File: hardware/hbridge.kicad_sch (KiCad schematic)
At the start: 11 parts, among them U601 BTS7960B, U602 BTS7960B

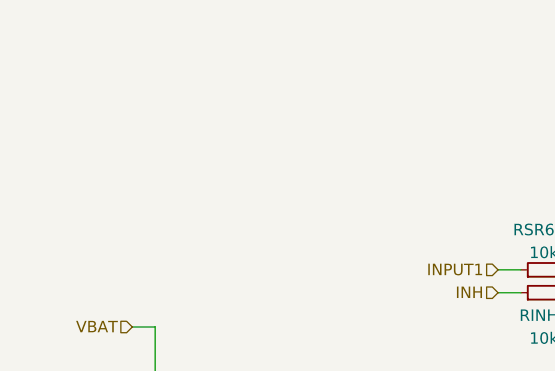
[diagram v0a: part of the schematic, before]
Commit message: Added analog stage for Vbat measurement, and it's simulation
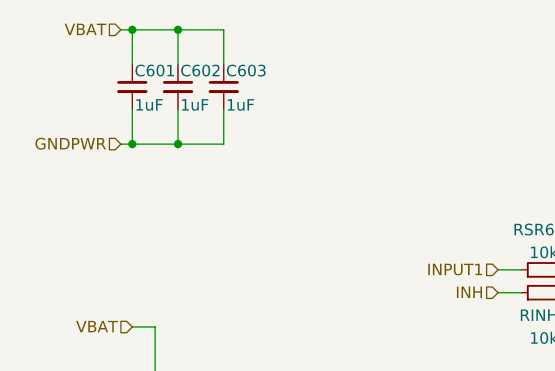
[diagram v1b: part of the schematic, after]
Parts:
- added C601, C602, C603: 1uF, Capacitor_SMD:C_1206_3216Metric_Pad1.33x1.80mm_HandSolder, symbol Device:C_Small
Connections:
- net GNDPWR: now also C601.2, C602.2, C603.2
- net VBAT: now also C601.1, C602.1, C603.1
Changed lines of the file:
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@@
 (kicad_sch (version 20211123) (generator eeschema)
   (paper "A4")
+  (junction (at 52.07 50.8) (diameter 0) (color 0 0 0 0)
+  )
+  (junction (at 57.15 38.1) (diameter 0) (color 0 0 0 0)
+  )
+  (junction (at 57.15 50.8) (diameter 0) (color 0 0 0 0)
+  )
   (junction (at 54.61 78.74) (diameter 0) (color 0 0 0 0)
   )
+  (junction (at 52.07 38.1) (diameter 0) (color 0 0 0 0)
+  )
   (junction (at 54.61 97.79) (diameter 0) (color 0 0 0 0)
   )
@@
     (stroke (width 0) (type default) (color 0 0 0 0))
   )
+  (wire (pts (xy 57.15 50.8) (xy 52.07 50.8))
+    (stroke (width 0) (type default) (color 0 0 0 0))
+  )
+  (wire (pts (xy 57.15 41.91) (xy 57.15 38.1))
+    (stroke (width 0) (type default) (color 0 0 0 0))
+  )
   (wire (pts (xy 54.61 71.12) (xy 52.07 71.12))
     (stroke (width 0) (type default) (color 0 0 0 0))
   )
+  (wire (pts (xy 62.23 38.1) (xy 62.23 41.91))
+    (stroke (width 0) (type default) (color 0 0 0 0))
+  )
   (wire (pts (xy 107.95 114.3) (xy 109.22 114.3))
     (stroke (width 0) (type default) (color 0 0 0 0))
@@
     (stroke (width 0) (type default) (color 0 0 0 0))
   )
+  (wire (pts (xy 52.07 46.99) (xy 52.07 50.8))
+    (stroke (width 0) (type default) (color 0 0 0 0))
+  )
   (wire (pts (xy 149.86 114.3) (xy 152.4 114.3))
     (stroke (width 0) (type default) (color 0 0 0 0))
@@
     (stroke (width 0) (type default) (color 0 0 0 0))
   )
+  (wire (pts (xy 50.8 38.1) (xy 52.07 38.1))
+    (stroke (width 0) (type default) (color 0 0 0 0))
+  )
+  (wire (pts (xy 57.15 38.1) (xy 62.23 38.1))
+    (stroke (width 0) (type default) (color 0 0 0 0))
+  )
   (wire (pts (xy 100.33 67.31) (xy 110.49 67.31))
     (stroke (width 0) (type default) (color 0 0 0 0))
@@
     (stroke (width 0) (type default) (color 0 0 0 0))
   )
+  (wire (pts (xy 62.23 46.99) (xy 62.23 50.8))
+    (stroke (width 0) (type default) (color 0 0 0 0))
+  )
   (wire (pts (xy 107.95 69.85) (xy 110.49 69.85))
     (stroke (width 0) (type default) (color 0 0 0 0))
@@
     (stroke (width 0) (type default) (color 0 0 0 0))
   )
+  (wire (pts (xy 57.15 46.99) (xy 57.15 50.8))
+    (stroke (width 0) (type default) (color 0 0 0 0))
+  )
   (wire (pts (xy 92.71 111.76) (xy 95.25 111.76))
     (stroke (width 0) (type default) (color 0 0 0 0))
@@
     (stroke (width 0) (type default) (color 0 0 0 0))
   )
+  (wire (pts (xy 52.07 41.91) (xy 52.07 38.1))
+    (stroke (width 0) (type default) (color 0 0 0 0))
+  )
   (wire (pts (xy 153.67 76.2) (xy 153.67 78.74))
     (stroke (width 0) (type default) (color 0 0 0 0))
@@
     (stroke (width 0) (type default) (color 0 0 0 0))
   )
+  (wire (pts (xy 52.07 38.1) (xy 57.15 38.1))
+    (stroke (width 0) (type default) (color 0 0 0 0))
+  )
   (wire (pts (xy 48.26 85.09) (xy 48.26 78.74))
     (stroke (width 0) (type default) (color 0 0 0 0))
@@
     (stroke (width 0) (type default) (color 0 0 0 0))
   )
+  (wire (pts (xy 62.23 50.8) (xy 57.15 50.8))
+    (stroke (width 0) (type default) (color 0 0 0 0))
+  )
   (wire (pts (xy 185.42 77.47) (xy 185.42 81.28))
+    (stroke (width 0) (type default) (color 0 0 0 0))
+  )
+  (wire (pts (xy 52.07 50.8) (xy 50.8 50.8))
     (stroke (width 0) (type default) (color 0 0 0 0))
   )
@@
     (effects (font (size 1.27 1.27)) (justify right))
   )
+  (hierarchical_label "VBAT" (shape input) (at 50.8 38.1 180)
+    (effects (font (size 1.27 1.27)) (justify right))
+  )
   (hierarchical_label "VBAT" (shape input) (at 52.07 71.12 180)
     (effects (font (size 1.27 1.27)) (justify right))
   )
+  (hierarchical_label "GNDPWR" (shape input) (at 50.8 50.8 180)
+    (effects (font (size 1.27 1.27)) (justify right))
+  )
   (hierarchical_label "IS" (shape input) (at 185.42 77.47 180)
     (effects (font (size 1.27 1.27)) (justify right))
@@
   (hierarchical_label "OUT2" (shape input) (at 107.95 93.98 180)
     (effects (font (size 1.27 1.27)) (justify right))
+  )
+  (symbol (lib_id "Device:C_Small") (at 57.15 44.45 0) (unit 1)
+    (in_bom yes) (on_board yes)
+    (property "Reference" "C602" (id 0) (at 57.404 42.672 0)
+      (effects (font (size 1.27 1.27)) (justify left))
+    )
+    (property "Value" "1uF" (id 1) (at 57.404 46.482 0)
+      (effects (font (size 1.27 1.27)) (justify left))
+    )
+    (property "Footprint" "Capacitor_SMD:C_1206_3216Metric_Pad1.33x1.80mm_HandSolder" (id 2) (at 57.15 44.45 0)
+      (effects (font (size 1.27 1.27)) hide)
+    )
+    (property "Datasheet" "" (id 3) (at 57.15 44.45 0)
+      (effects (font (size 1.27 1.27)) hide)
+    )
+    (pin "1")
+    (pin "2")
   )
   (symbol (lib_id "power:GND") (at 185.42 88.9 0) (unit 1)
@@
     (pin "2")
   )
+  (symbol (lib_id "Device:C_Small") (at 52.07 44.45 0) (unit 1)
+    (in_bom yes) (on_board yes)
+    (property "Reference" "C601" (id 0) (at 52.324 42.672 0)
+      (effects (font (size 1.27 1.27)) (justify left))
+    )
+    (property "Value" "1uF" (id 1) (at 52.324 46.482 0)
+      (effects (font (size 1.27 1.27)) (justify left))
+    )
+    (property "Footprint" "Capacitor_SMD:C_1206_3216Metric_Pad1.33x1.80mm_HandSolder" (id 2) (at 52.07 44.45 0)
+      (effects (font (size 1.27 1.27)) hide)
+    )
+    (property "Datasheet" "" (id 3) (at 52.07 44.45 0)
+      (effects (font (size 1.27 1.27)) hide)
+    )
+    (pin "1")
+    (pin "2")
+  )
   (symbol (lib_id "Device:R_Small") (at 97.79 64.77 90) (unit 1)
     (in_bom yes) (on_board yes) (fields_autoplaced)
@@
       (effects (font (size 1.27 1.27)) hide)
     )
+    (pin "1")
+    (pin "2")
+  )
+  (symbol (lib_id "Device:C_Small") (at 62.23 44.45 0) (unit 1)
+    (in_bom yes) (on_board yes)
+    (property "Reference" "C603" (id 0) (at 62.484 42.672 0)
+      (effects (font (size 1.27 1.27)) (justify left))
+    )
+    (property "Value" "1uF" (id 1) (at 62.484 46.482 0)
+      (effects (font (size 1.27 1.27)) (justify left))
+    )
+    (property "Footprint" "Capacitor_SMD:C_1206_3216Metric_Pad1.33x1.80mm_HandSolder" (id 2) (at 62.23 44.45 0)
+      (effects (font (size 1.27 1.27)) hide)
+    )
+    (property "Datasheet" "" (id 3) (at 62.23 44.45 0)
+      (effects (font (size 1.27 1.27)) hide)
+    )

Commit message: hardware: K78L15 to supply INA826 and other changes
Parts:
- added C604: (no value), symbol Device:C_Polarized_Small
- added C605, C606: C_Polarized_Small, Capacitor_SMD:CP_Elec_8x10, symbol Device:C_Polarized_Small
- added RIS601: (no value), symbol Device:R_Small
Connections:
- net GND: now also RIS601.2
- net GNDPWR: now also C604.2, C605.2, C606.2
- net VBAT: now also C604.1, C605.1, C606.1
- net IS renamed IS1
- net IS1: no longer U602.6 (IS)
- new net IS2: RIS601.1, U602.6 (IS)
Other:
- moved on the sheet: RIS1

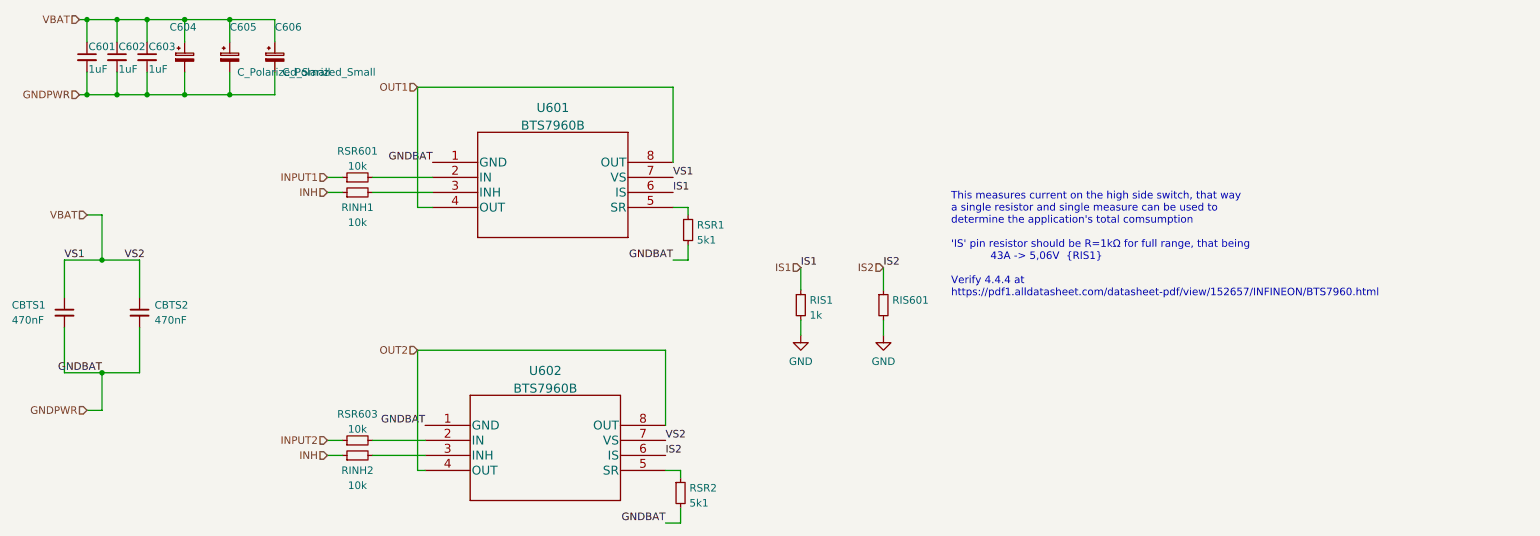
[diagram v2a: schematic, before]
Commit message: hardware: silkscreen updated with JLC. Finished.
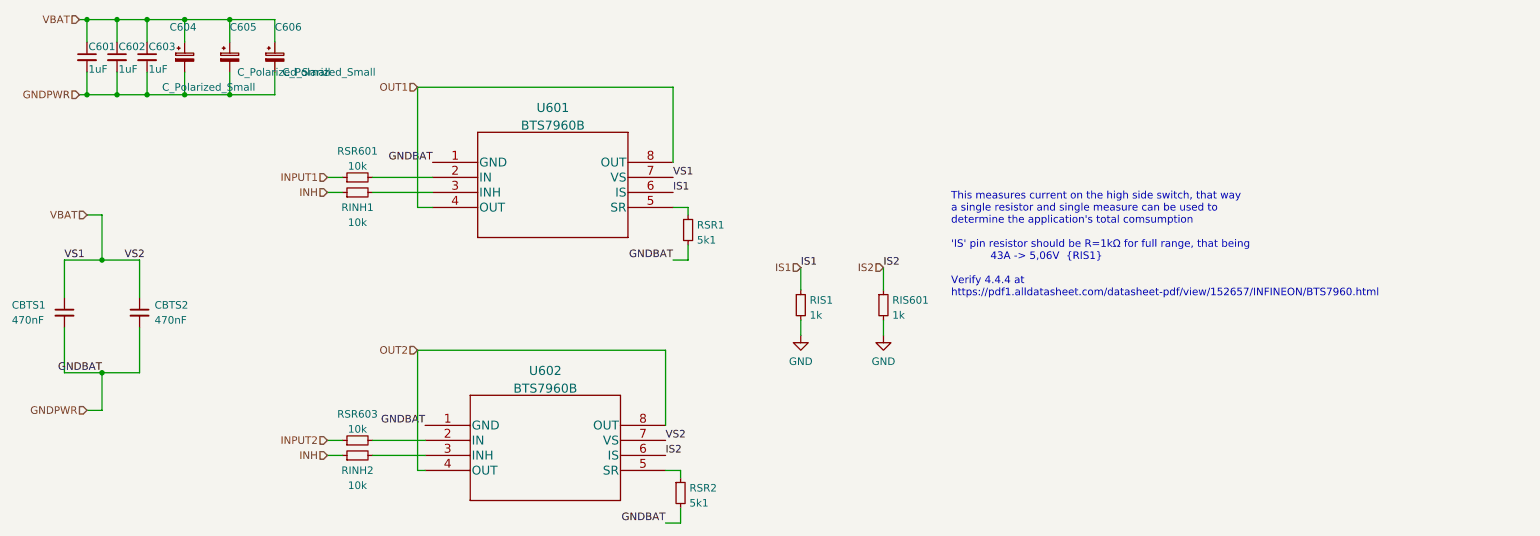
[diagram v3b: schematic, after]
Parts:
- C604: value (none) -> C_Polarized_Small; footprint (none) -> Capacitor_SMD:CP_Elec_8x10
- RIS601: value (none) -> 1k; footprint (none) -> Resistor_SMD:R_0805_2012Metric_Pad1.20x1.40mm_HandSolder
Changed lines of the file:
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@@
       (effects (font (size 1.27 1.27)) (justify left))
     )
-    (property "Value" "" (id 1) (at 64.77 49.53 0)
-      (effects (font (size 1.27 1.27)) (justify left))
-    )
-    (property "Footprint" "" (id 2) (at 68.58 44.45 0)
+    (property "Value" "C_Polarized_Small" (id 1) (at 64.77 49.53 0)
+      (effects (font (size 1.27 1.27)) (justify left))
+    )
+    (property "Footprint" "Capacitor_SMD:CP_Elec_8x10" (id 2) (at 68.58 44.45 0)
       (effects (font (size 1.27 1.27)) hide)
     )
@@
       (effects (font (size 1.27 1.27)) (justify left))
     )
-    (property "Value" "" (id 1) (at 188.1886 88.0622 0)
-      (effects (font (size 1.27 1.27)) (justify left))
-    )
-    (property "Footprint" "" (id 2) (at 186.69 86.36 0)
-      (effects (font (size 1.27 1.27)) hide)
-    )
+    (property "Value" "1k" (id 1) (at 188.1886 88.0622 0)
+      (effects (font (size 1.27 1.27)) (justify left))
+    )
+    (property "Footprint" "Resistor_SMD:R_0805_2012Metric_Pad1.20x1.40mm_HandSolder" (id 2) (at 186.69 86.36 0)
+      (effects (font (size 1.27 1.27)) hide)
+    )
